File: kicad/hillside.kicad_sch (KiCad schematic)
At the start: 65 parts, among them J1 Haptic, J2 TRRS, J3 Bat_Pos, J4 Bat_GND, K1 SW_Key, K10 SW_Key, K11 SW_Key, K12 SW_Key, K13 SW_Key, K14 SW_Key, K15 SW_Key, K16 SW_Key, K17 SW_Key, K18 SW_Key, K19 SW_Key, K2 SW_Key, K20 SW_Rotary, K21 SW_Key, K22 SW_Key, K23 SW_Key, K24 SW_Key, K3 SW_Key, K4 SW_Key, K5 SW_Key, K6 SW_Key, K7 SW_Key, K8 SW_Key, K9 SW_Key, SW1 Reset, SW2 SW_Power, U1 ProMicro_r

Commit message: schema: Remove mounting holes for breakaway slot
- extra stitching via
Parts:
- removed H6, H7: MountHole, MountingHole:MountingHole_2.2mm_M2, symbol Mechanical:MountingHole
- added V1: Via, hillside_basic:VIA-0.8mm, symbol hillside_basic:Via
- renumbered H8 to H6, H9 to H7
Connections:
- net GND: now also V1.1 (via)
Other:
- moved on the sheet: H1, H2, H4, H5
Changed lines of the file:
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@@
   (junction (at 218.44 162.56) (diameter 0) (color 0 0 0 0)
+  )
+  (junction (at 236.22 36.83) (diameter 0) (color 0 0 0 0)
   )
   (no_connect (at 83.82 139.7))
@@
     (stroke (width 0) (type default) (color 0 0 0 0))
   )
+  (wire (pts (xy 236.22 36.83) (xy 240.03 36.83))
+    (stroke (width 0) (type default) (color 0 0 0 0))
+  )
   (wire (pts (xy 162.56 50.8) (xy 162.56 48.26))
     (stroke (width 0) (type default) (color 0 0 0 0))
@@
     (stroke (width 0) (type default) (color 0 0 0 0))
   )
-  (wire (pts (xy 231.14 36.83) (xy 240.03 36.83))
+  (wire (pts (xy 231.14 36.83) (xy 236.22 36.83))
     (stroke (width 0) (type default) (color 0 0 0 0))
   )
@@
     (pin "1")
   )
-  (symbol (lib_id "hillside:Mount_Tenting") (at 248.92 116.84 0) (unit 1)
-    (in_bom yes) (on_board yes)
-    (property "Reference" "H1" (id 0) (at 252.73 114.935 0)
+  (symbol (lib_id "hillside:Mount_Tenting") (at 248.92 121.92 0) (unit 1)
+    (in_bom yes) (on_board yes)
+    (property "Reference" "H1" (id 0) (at 252.73 120.015 0)
       (effects (font (size 1.27 1.27)) (justify left top))
     )
-    (property "Value" "Mount_Tenting" (id 1) (at 252.73 118.745 0)
+    (property "Value" "Mount_Tenting" (id 1) (at 252.73 123.825 0)
       (effects (font (size 1.27 1.27)) (justify left bottom))
     )
-    (property "Footprint" "hillside:Tenting_Puck" (id 2) (at 248.92 116.84 0)
-      (effects (font (size 1.27 1.27)) hide)
-    )
-    (property "Datasheet" "" (id 3) (at 248.92 116.84 0)
-      (effects (font (size 1.27 1.27)) hide)
-    )
-  )
-  (symbol (lib_id "hillside:Mount_Trackball") (at 229.87 116.84 0) (unit 1)
-    (in_bom yes) (on_board yes)
-    (property "Reference" "H2" (id 0) (at 233.045 116.205 0)
-      (effects (font (size 1.27 1.27)) (justify left))
-    )
-    (property "Value" "Trackball" (id 1) (at 233.045 118.11 0)
-      (effects (font (size 1.27 1.27)) (justify left))
-    )
-    (property "Footprint" "hillside:Pimoroni_Trackball" (id 2) (at 233.045 116.205 0)
-      (effects (font (size 1.27 1.27)) hide)
-    )
-    (property "Datasheet" "" (id 3) (at 233.045 116.205 0)
+    (property "Footprint" "hillside:Tenting_Puck" (id 2) (at 248.92 121.92 0)
+      (effects (font (size 1.27 1.27)) hide)
+    )
+    (property "Datasheet" "" (id 3) (at 248.92 121.92 0)
+      (effects (font (size 1.27 1.27)) hide)
+    )
+  )
+  (symbol (lib_id "hillside:Mount_Trackball") (at 229.87 121.92 0) (unit 1)
+    (in_bom yes) (on_board yes)
+    (property "Reference" "H2" (id 0) (at 233.045 121.285 0)
+      (effects (font (size 1.27 1.27)) (justify left))
+    )
+    (property "Value" "Trackball" (id 1) (at 233.045 123.19 0)
+      (effects (font (size 1.27 1.27)) (justify left))
+    )
+    (property "Footprint" "hillside:Pimoroni_Trackball" (id 2) (at 233.045 121.285 0)
+      (effects (font (size 1.27 1.27)) hide)
+    )
+    (property "Datasheet" "" (id 3) (at 233.045 121.285 0)
       (effects (font (size 1.27 1.27)) hide)
     )
@@
     )
   )
-  (symbol (lib_id "Mechanical:MountingHole") (at 248.92 125.73 0) (unit 1)
-    (in_bom yes) (on_board yes)
-    (property "Reference" "H5" (id 0) (at 251.46 124.46 0)
-      (effects (font (size 1.27 1.27)) (justify left))
-    )
-    (property "Value" "MountHole" (id 1) (at 251.46 125.73 0)
-      (effects (font (size 1.27 1.27)) (justify left))
-    )
-    (property "Footprint" "MountingHole:MountingHole_2.2mm_M2_Pad" (id 2) (at 248.92 125.73 0)
-      (effects (font (size 1.27 1.27)) hide)
-    )
-    (property "Datasheet" "~" (id 3) (at 248.92 125.73 0)
-      (effects (font (size 1.27 1.27)) hide)
-    )
-  )
-  (symbol (lib_id "Mechanical:MountingHole") (at 248.92 130.81 0) (unit 1)
-    (in_bom yes) (on_board yes)
-    (property "Reference" "H7" (id 0) (at 251.46 129.54 0)
-      (effects (font (size 1.27 1.27)) (justify left))
-    )
-    (property "Value" "MountHole" (id 1) (at 251.46 130.81 0)
-      (effects (font (size 1.27 1.27)) (justify left))
-    )
-    (property "Footprint" "MountingHole:MountingHole_2.2mm_M2" (id 2) (at 248.92 130.81 0)
-      (effects (font (size 1.27 1.27)) hide)
-    )
-    (property "Datasheet" "~" (id 3) (at 248.92 130.81 0)
-      (effects (font (size 1.27 1.27)) hide)
-    )
-  )
-  (symbol (lib_id "Mechanical:MountingHole") (at 229.87 125.73 0) (unit 1)
-    (in_bom yes) (on_board yes)
-    (property "Reference" "H4" (id 0) (at 232.41 124.46 0)
-      (effects (font (size 1.27 1.27)) (justify left))
-    )
-    (property "Value" "MountHole" (id 1) (at 232.41 125.73 0)
-      (effects (font (size 1.27 1.27)) (justify left))
-    )
-    (property "Footprint" "MountingHole:MountingHole_2.2mm_M2_Pad" (id 2) (at 229.87 125.73 0)
-      (effects (font (size 1.27 1.27)) hide)
-    )
-    (property "Datasheet" "~" (id 3) (at 229.87 125.73 0)
-      (effects (font (size 1.27 1.27)) hide)
-    )
-  )
-  (symbol (lib_id "Mechanical:MountingHole") (at 229.87 130.81 0) (unit 1)
-    (in_bom yes) (on_board yes)
-    (property "Reference" "H6" (id 0) (at 232.41 129.54 0)
-      (effects (font (size 1.27 1.27)) (justify left))
-    )
-    (property "Value" "MountHole" (id 1) (at 232.41 130.81 0)
-      (effects (font (size 1.27 1.27)) (justify left))
-    )
-    (property "Footprint" "MountingHole:MountingHole_2.2mm_M2" (id 2) (at 229.87 130.81 0)
-      (effects (font (size 1.27 1.27)) hide)
-    )
-    (property "Datasheet" "~" (id 3) (at 229.87 130.81 0)
+  (symbol (lib_id "Mechanical:MountingHole") (at 248.92 129.54 0) (unit 1)
+    (in_bom yes) (on_board yes)
+    (property "Reference" "H5" (id 0) (at 251.46 128.27 0)
+      (effects (font (size 1.27 1.27)) (justify left))
+    )
+    (property "Value" "MountHole" (id 1) (at 251.46 129.54 0)
+      (effects (font (size 1.27 1.27)) (justify left))
+    )
+    (property "Footprint" "MountingHole:MountingHole_2.2mm_M2_Pad" (id 2) (at 248.92 129.54 0)
+      (effects (font (size 1.27 1.27)) hide)
+    )
+    (property "Datasheet" "~" (id 3) (at 248.92 129.54 0)
+      (effects (font (size 1.27 1.27)) hide)
+    )
+  )
+  (symbol (lib_id "Mechanical:MountingHole") (at 229.87 129.54 0) (unit 1)
+    (in_bom yes) (on_board yes)
+    (property "Reference" "H4" (id 0) (at 232.41 128.27 0)
+      (effects (font (size 1.27 1.27)) (justify left))
+    )
+    (property "Value" "MountHole" (id 1) (at 232.41 129.54 0)
+      (effects (font (size 1.27 1.27)) (justify left))
+    )
+    (property "Footprint" "MountingHole:MountingHole_2.2mm_M2_Pad" (id 2) (at 229.87 129.54 0)
+      (effects (font (size 1.27 1.27)) hide)
+    )
+    (property "Datasheet" "~" (id 3) (at 229.87 129.54 0)
       (effects (font (size 1.27 1.27)) hide)
     )
@@
   (symbol (lib_id "Mechanical:MountingHole") (at 229.87 135.89 0) (unit 1)
     (in_bom yes) (on_board yes)
-    (property "Reference" "H8" (id 0) (at 232.41 134.62 0)
+    (property "Reference" "H6" (id 0) (at 232.41 134.62 0)
       (effects (font (size 1.27 1.27)) (justify left))
     )
@@
   (symbol (lib_id "Mechanical:MountingHole") (at 248.92 135.89 0) (unit 1)
     (in_bom yes) (on_board yes)
-    (property "Reference" "H9" (id 0) (at 251.46 134.62 0)
+    (property "Reference" "H7" (id 0) (at 251.46 134.62 0)
       (effects (font (size 1.27 1.27)) (justify left))
     )
@@
       (effects (font (size 1.27 1.27)) hide)
     )
+  )
+  (symbol (lib_id "hillside_basic:Via") (at 236.22 36.83 270) (unit 1)
+    (in_bom yes) (on_board yes)
+    (property "Reference" "V1" (id 0) (at 236.22 41.91 0)
+      (effects (font (size 1.27 1.27)) (justify bottom) hide)
+    )
+    (property "Value" "Via" (id 1) (at 229.87 36.83 0)
+      (effects (font (size 1.27 1.27)) hide)
+    )
+    (property "Footprint" "hillside_basic:VIA-0.8mm" (id 2) (at 233.68 36.83 0)
+      (effects (font (size 1.27 1.27)) hide)
+    )
+    (property "Datasheet" "" (id 3) (at 236.22 36.83 0)
+      (effects (font (size 1.27 1.27)) hide)
+    )
+    (pin "1")
   )
   (sheet_instances
@@
       (reference "H5") (unit 1) (value "MountHole") (footprint "MountingHole:MountingHole_2.2mm_M2_Pad")
     )
-    (path "/00000000-0000-0000-0000-00006219aacc"
-      (reference "H6") (unit 1) (value "MountHole") (footprint "MountingHole:MountingHole_2.2mm_M2")
-    )
-    (path "/00000000-0000-0000-0000-00006218a790"
-      (reference "H7") (unit 1) (value "MountHole") (footprint "MountingHole:MountingHole_2.2mm_M2")
-    )
     (path "/00000000-0000-0000-0000-0000621ecfae"
-      (reference "H8") (unit 1) (value "MountHole") (footprint "MountingHole:MountingHole_2.2mm_M2_Pad")
+      (reference "H6") (unit 1) (value "MountHole") (footprint "MountingHole:MountingHole_2.2mm_M2_Pad")
     )
     (path "/00000000-0000-0000-0000-0000621fdcbf"
-      (reference "H9") (unit 1) (value "MountHole") (footprint "MountingHole:MountingHole_2.2mm_M2_Pad")
+      (reference "H7") (unit 1) (value "MountHole") (footprint "MountingHole:MountingHole_2.2mm_M2_Pad")
     )
     (path "/00000000-0000-0000-0000-0000616b8147"
@@
       (reference "U1") (unit 1) (value "ProMicro_r") (footprint "hillside:ProMicro_v2")
     )
+    (path "/28a7bffd-830a-4229-bae4-fa3de7e1fd6b"
+      (reference "V1") (unit 1) (value "Via") (footprint "hillside_basic:VIA-0.8mm")
+    )
     (path "/00000000-0000-0000-0000-0000615e1c4e"

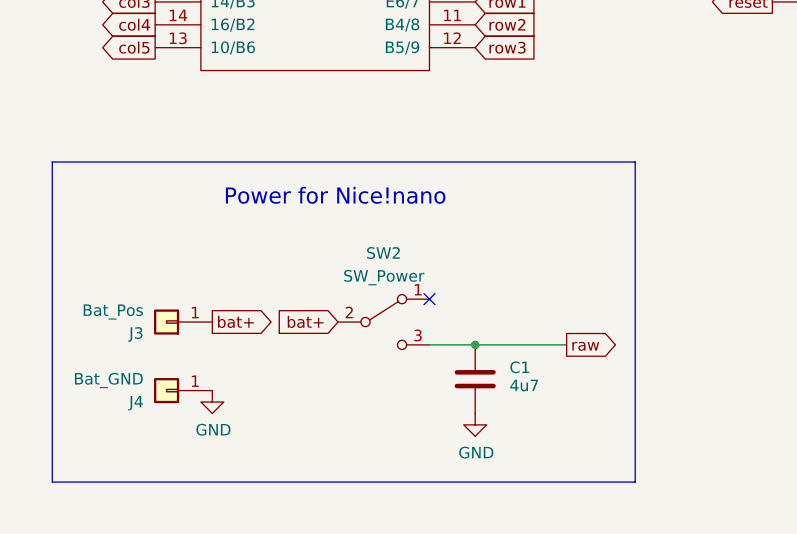
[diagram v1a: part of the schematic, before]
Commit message: Two battery pad options. PCB to MCU alignment note
- Clearer track routing, Parallel tracks split into groups by function,
  not all clumped.
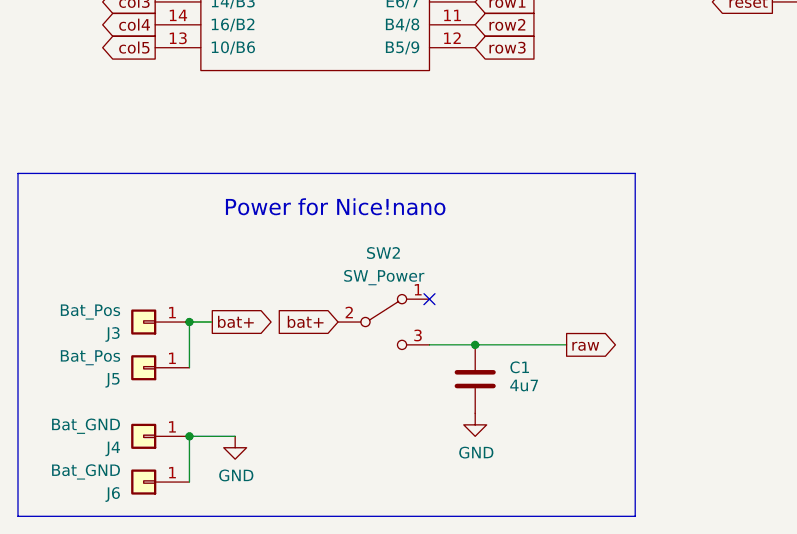
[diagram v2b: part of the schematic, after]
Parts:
- added J5: Bat_Pos, hillside_basic:1pin_conn, symbol Connector_Generic:Conn_01x01
- added J6: Bat_GND, hillside_basic:1pin_conn, symbol Connector_Generic:Conn_01x01
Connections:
- net GND: now also J6.1 (Pin_1)
- net bat+: now also J5.1 (Pin_1)
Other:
- moved on the sheet: J3, J4
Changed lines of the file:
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@@
   (junction (at 243.84 36.83) (diameter 0) (color 0 0 0 0)
   )
+  (junction (at 52.07 193.04) (diameter 0) (color 0 0 0 0)
+  )
   (junction (at 48.26 71.12) (diameter 0) (color 0 0 0 0)
   )
@@
   )
   (junction (at 88.9 57.15) (diameter 0) (color 0 0 0 0)
+  )
+  (junction (at 52.07 180.34) (diameter 0) (color 0 0 0 0)
   )
   (junction (at 172.72 127) (diameter 0) (color 0 0 0 0)
@@
     (stroke (width 0) (type default) (color 0 0 0 0))
   )
-  (polyline (pts (xy 101.6 162.56) (xy 36.83 162.56))
+  (polyline (pts (xy 101.6 163.83) (xy 33.02 163.83))
     (stroke (width 0) (type default) (color 0 0 0 0))
   )
@@
     (stroke (width 0) (type default) (color 0 0 0 0))
   )
-  (polyline (pts (xy 36.83 162.56) (xy 36.83 198.12))
+  (polyline (pts (xy 33.02 163.83) (xy 33.02 201.93))
     (stroke (width 0) (type default) (color 0 0 0 0))
   )
@@
     (stroke (width 0) (type default) (color 0 0 0 0))
   )
+  (wire (pts (xy 52.07 193.04) (xy 52.07 198.12))
+    (stroke (width 0) (type default) (color 0 0 0 0))
+  )
   (wire (pts (xy 144.78 39.37) (xy 157.48 39.37))
     (stroke (width 0) (type default) (color 0 0 0 0))
@@
     (stroke (width 0) (type default) (color 0 0 0 0))
   )
-  (polyline (pts (xy 101.6 198.12) (xy 101.6 162.56))
+  (polyline (pts (xy 101.6 201.93) (xy 101.6 163.83))
     (stroke (width 0) (type default) (color 0 0 0 0))
   )
@@
     (stroke (width 0) (type default) (color 0 0 0 0))
   )
+  (wire (pts (xy 52.07 180.34) (xy 54.61 180.34))
+    (stroke (width 0) (type default) (color 0 0 0 0))
+  )
   (wire (pts (xy 173.99 34.29) (xy 162.56 34.29))
     (stroke (width 0) (type default) (color 0 0 0 0))
@@
     (stroke (width 0) (type default) (color 0 0 0 0))
   )
-  (polyline (pts (xy 36.83 198.12) (xy 101.6 198.12))
+  (polyline (pts (xy 33.02 201.93) (xy 101.6 201.93))
     (stroke (width 0) (type default) (color 0 0 0 0))
   )
@@
     (stroke (width 0) (type default) (color 0 0 0 0))
   )
+  (wire (pts (xy 52.07 180.34) (xy 52.07 185.42))
+    (stroke (width 0) (type default) (color 0 0 0 0))
+  )
   (wire (pts (xy 91.44 85.09) (xy 93.98 86.36))
     (stroke (width 0) (type default) (color 0 0 0 0))
@@
   )
   (wire (pts (xy 81.28 62.23) (xy 81.28 64.77))
+    (stroke (width 0) (type default) (color 0 0 0 0))
+  )
+  (wire (pts (xy 52.07 193.04) (xy 57.15 193.04))
     (stroke (width 0) (type default) (color 0 0 0 0))
   )
@@
     (effects (font (size 1.778 1.778)) (justify left bottom))
   )
-  (text "Power for Nice!nano" (at 55.88 167.64 0)
+  (text "Power for Nice!nano" (at 55.88 168.91 0)
     (effects (font (size 1.778 1.778)) (justify left bottom))
   )
@@
     (pin "3")
   )
-  (symbol (lib_id "Connector_Generic:Conn_01x01") (at 49.53 180.34 180) (unit 1)
-    (in_bom yes) (on_board yes)
-    (property "Reference" "J3" (id 0) (at 46.99 181.61 0)
-      (effects (font (size 1.27 1.27)) (justify left))
-    )
-    (property "Value" "Bat_Pos" (id 1) (at 46.99 179.07 0)
-      (effects (font (size 1.27 1.27)) (justify left))
-    )
-    (property "Footprint" "hillside_basic:1pin_conn" (id 2) (at 49.53 180.34 0)
-      (effects (font (size 1.27 1.27)) hide)
-    )
-    (property "Datasheet" "~" (id 3) (at 49.53 180.34 0)
-      (effects (font (size 1.27 1.27)) hide)
-    )
-    (pin "1")
-  )
-  (symbol (lib_id "Connector_Generic:Conn_01x01") (at 49.53 187.96 180) (unit 1)
-    (in_bom yes) (on_board yes)
-    (property "Reference" "J4" (id 0) (at 46.99 189.23 0)
-      (effects (font (size 1.27 1.27)) (justify left))
-    )
-    (property "Value" "Bat_GND" (id 1) (at 46.99 186.69 0)
-      (effects (font (size 1.27 1.27)) (justify left))
-    )
-    (property "Footprint" "hillside_basic:1pin_conn" (id 2) (at 49.53 187.96 0)
-      (effects (font (size 1.27 1.27)) hide)
-    )
-    (property "Datasheet" "~" (id 3) (at 49.53 187.96 0)
-      (effects (font (size 1.27 1.27)) hide)
-    )
-    (pin "1")
-  )
-  (symbol (lib_id "power:GND") (at 54.61 187.96 0) (unit 1)
-    (in_bom yes) (on_board yes)
-    (property "Reference" "#PWR01" (id 0) (at 54.61 194.31 0)
-      (effects (font (size 1.27 1.27)) hide)
-    )
-    (property "Value" "GND" (id 1) (at 54.737 192.3542 0))
-    (property "Footprint" "" (id 2) (at 54.61 187.96 0)
-      (effects (font (size 1.27 1.27)) hide)
-    )
-    (property "Datasheet" "" (id 3) (at 54.61 187.96 0)
+  (symbol (lib_id "Connector_Generic:Conn_01x01") (at 46.99 180.34 180) (unit 1)
+    (in_bom yes) (on_board yes)
+    (property "Reference" "J3" (id 0) (at 44.45 181.61 0)
+      (effects (font (size 1.27 1.27)) (justify left))
+    )
+    (property "Value" "Bat_Pos" (id 1) (at 44.45 179.07 0)
+      (effects (font (size 1.27 1.27)) (justify left))
+    )
+    (property "Footprint" "hillside_basic:1pin_conn" (id 2) (at 46.99 180.34 0)
+      (effects (font (size 1.27 1.27)) hide)
+    )
+    (property "Datasheet" "~" (id 3) (at 46.99 180.34 0)
+      (effects (font (size 1.27 1.27)) hide)
+    )
+    (pin "1")
+  )
+  (symbol (lib_id "Connector_Generic:Conn_01x01") (at 46.99 193.04 180) (unit 1)
+    (in_bom yes) (on_board yes)
+    (property "Reference" "J4" (id 0) (at 44.45 194.31 0)
+      (effects (font (size 1.27 1.27)) (justify left))
+    )
+    (property "Value" "Bat_GND" (id 1) (at 44.45 191.77 0)
+      (effects (font (size 1.27 1.27)) (justify left))
+    )
+    (property "Footprint" "hillside_basic:1pin_conn" (id 2) (at 46.99 193.04 0)
+      (effects (font (size 1.27 1.27)) hide)
+    )
+    (property "Datasheet" "~" (id 3) (at 46.99 193.04 0)
+      (effects (font (size 1.27 1.27)) hide)
+    )
+    (pin "1")
+  )
+  (symbol (lib_id "power:GND") (at 57.15 193.04 0) (unit 1)
+    (in_bom yes) (on_board yes)
+    (property "Reference" "#PWR01" (id 0) (at 57.15 199.39 0)
+      (effects (font (size 1.27 1.27)) hide)
+    )
+    (property "Value" "GND" (id 1) (at 57.277 197.4342 0))
+    (property "Footprint" "" (id 2) (at 57.15 193.04 0)
+      (effects (font (size 1.27 1.27)) hide)
+    )
+    (property "Datasheet" "" (id 3) (at 57.15 193.04 0)
       (effects (font (size 1.27 1.27)) hide)
     )
@@
     (pin "1")
   )
+  (symbol (lib_id "Connector_Generic:Conn_01x01") (at 46.99 198.12 180) (unit 1)
+    (in_bom yes) (on_board yes)
+    (property "Reference" "J6" (id 0) (at 44.45 199.39 0)
+      (effects (font (size 1.27 1.27)) (justify left))
+    )
+    (property "Value" "Bat_GND" (id 1) (at 44.45 196.85 0)
+      (effects (font (size 1.27 1.27)) (justify left))
+    )
+    (property "Footprint" "hillside_basic:1pin_conn" (id 2) (at 46.99 198.12 0)
+      (effects (font (size 1.27 1.27)) hide)
+    )
+    (property "Datasheet" "~" (id 3) (at 46.99 198.12 0)
+      (effects (font (size 1.27 1.27)) hide)
+    )
+    (pin "1")
+  )
+  (symbol (lib_id "Connector_Generic:Conn_01x01") (at 46.99 185.42 180) (unit 1)
+    (in_bom yes) (on_board yes)
+    (property "Reference" "J5" (id 0) (at 44.45 186.69 0)
+      (effects (font (size 1.27 1.27)) (justify left))
+    )
+    (property "Value" "Bat_Pos" (id 1) (at 44.45 184.15 0)
+      (effects (font (size 1.27 1.27)) (justify left))
+    )
+    (property "Footprint" "hillside_basic:1pin_conn" (id 2) (at 46.99 185.42 0)
+      (effects (font (size 1.27 1.27)) hide)
+    )
+    (property "Datasheet" "~" (id 3) (at 46.99 185.42 0)
+      (effects (font (size 1.27 1.27)) hide)
+    )
+    (pin "1")
+  )
   (sheet_instances
     (path "/" (page "1"))
@@
       (reference "J4") (unit 1) (value "Bat_GND") (footprint "hillside_basic:1pin_conn")
     )
+    (path "/dcd3d67b-68f6-4254-9704-f2476d5d4bf7"
+      (reference "J5") (unit 1) (value "Bat_Pos") (footprint "hillside_basic:1pin_conn")
+    )
+    (path "/7fe750fa-fb79-4107-b5d4-b2d926ec773d"
+      (reference "J6") (unit 1) (value "Bat_GND") (footprint "hillside_basic:1pin_conn")
+    )
     (path "/00000000-0000-0000-0000-000061a8564f"
